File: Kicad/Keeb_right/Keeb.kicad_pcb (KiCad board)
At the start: 2 copper layers, 118 x 118 mm, 23 parts, among them J1 MJ-4PP-9, SW1 CherryMX, SW10 CherryMX, SW11 CherryMX, SW12 CherryMX, SW13 CherryMX, SW14 CherryMX, SW15 CherryMX, SW16 CherryMX, SW17 CherryMX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

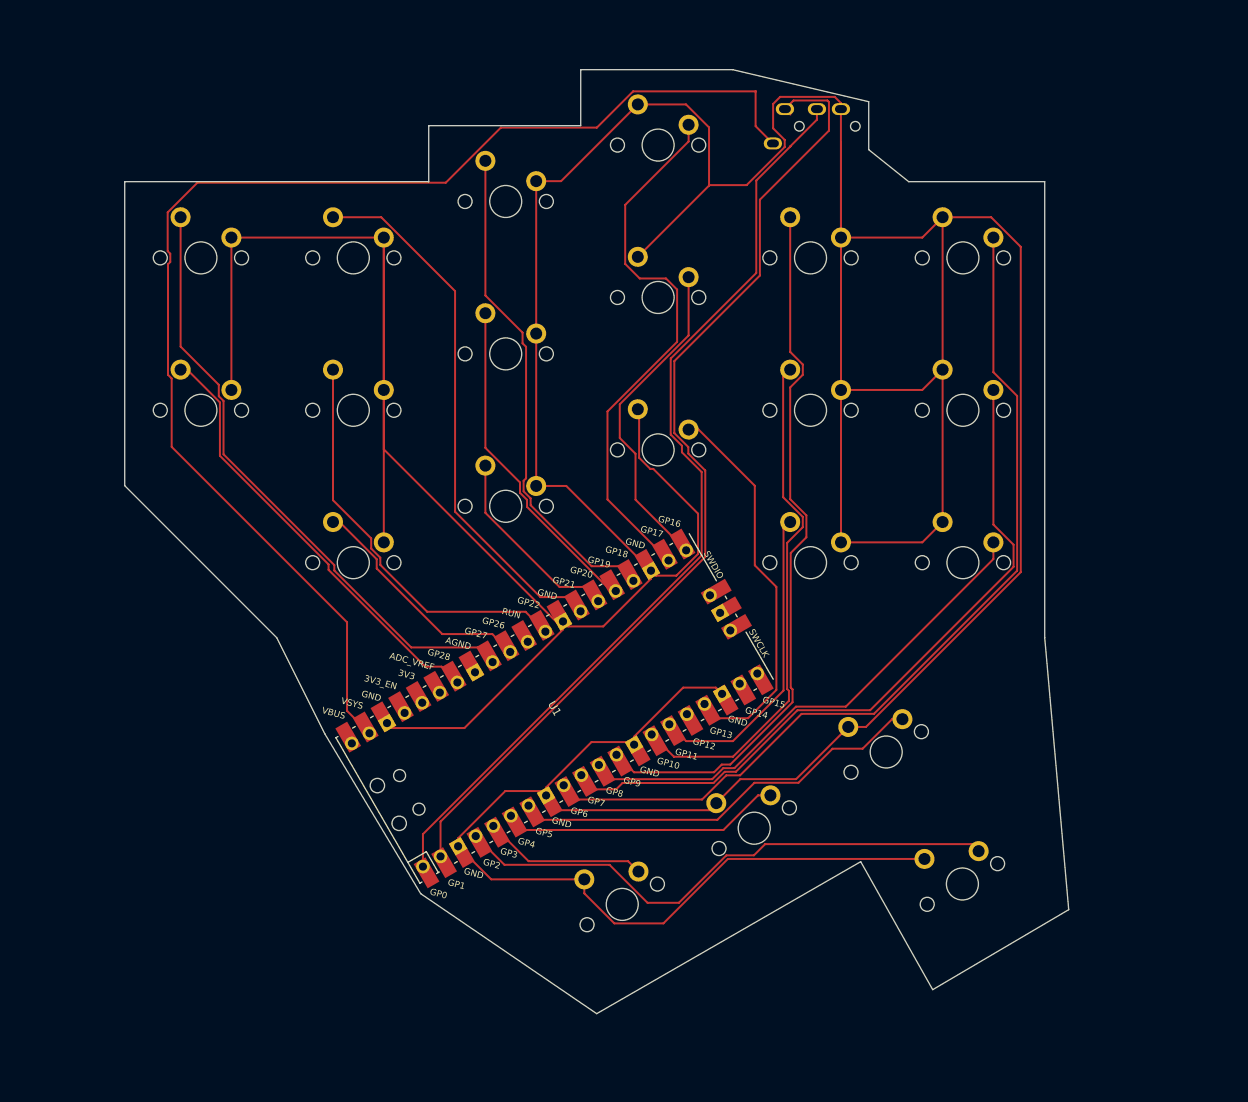
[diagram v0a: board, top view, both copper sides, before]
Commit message: spaced out tracks
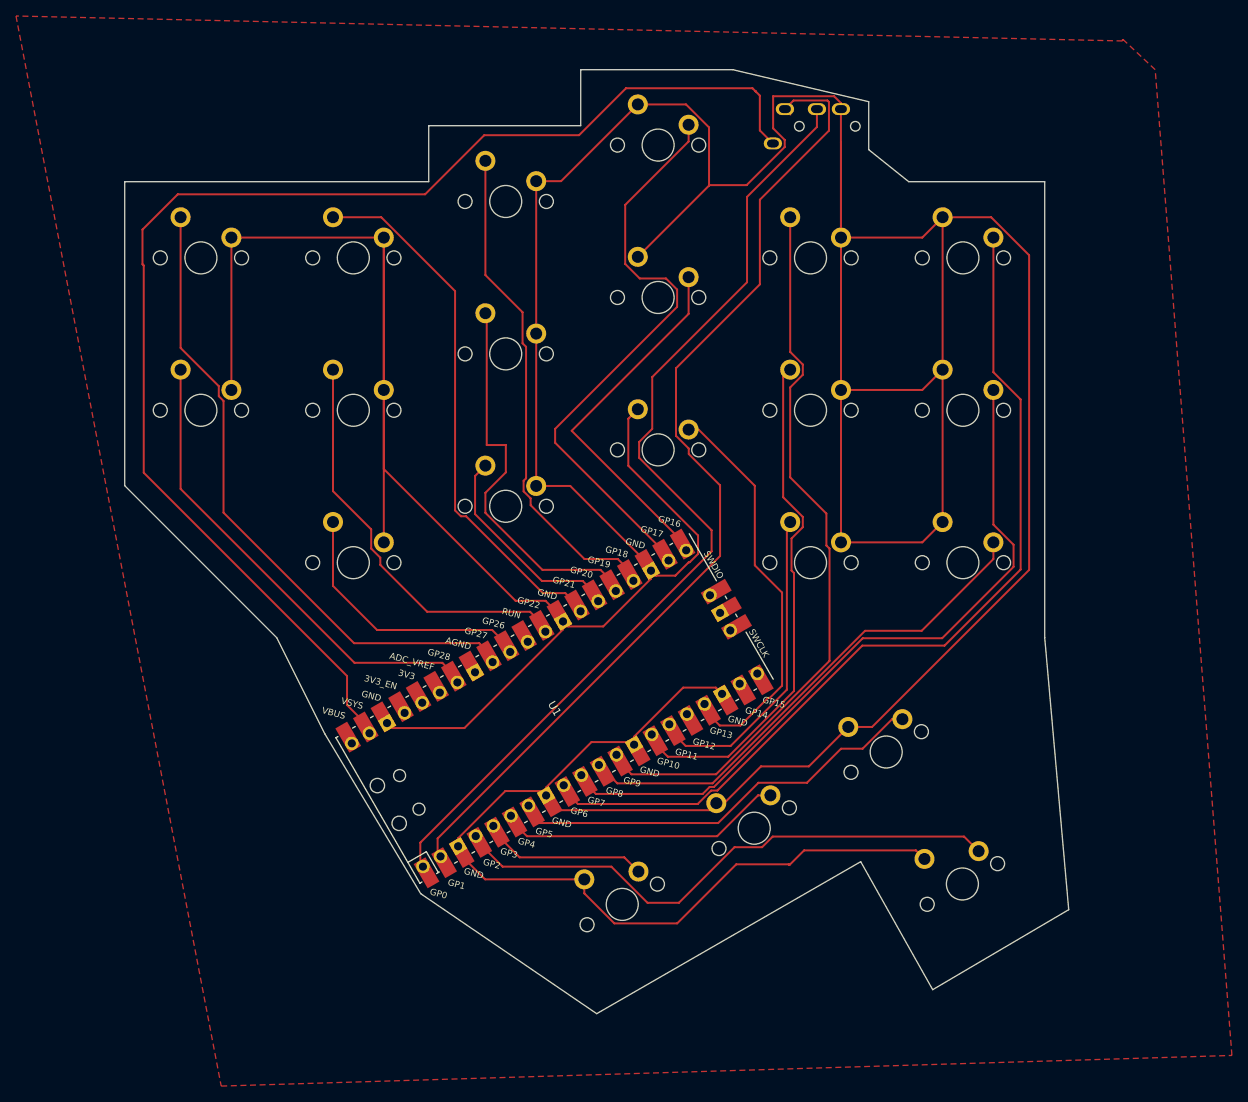
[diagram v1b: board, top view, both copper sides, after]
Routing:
- net 19: track 41.8 -> 49.2 mm
- net GND: track 717.0 -> 723.1 mm
- net 17: track 69.1 -> 74.6 mm
- net 16: track 41.2 -> 46.1 mm
- net 28: track 55.1 -> 59.9 mm
- net 0: track 118.3 -> 122.9 mm
- net 26: track 29.6 -> 33.8 mm
- net 27: track 76.6 -> 80.9 mm
- net 3v3: track 163.0 -> 166.3 mm
- net 9: track 90.2 -> 92.6 mm
- net 20: track 24.6 -> 26.8 mm
- net 13: track 49.0 -> 50.9 mm
- net 1: track 124.6 -> 126.3 mm
- net 6: track 117.0 -> 115.8 mm
- net 11: track 39.2 -> 40.2 mm
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- added copper zone on F.Cu, net (none)
